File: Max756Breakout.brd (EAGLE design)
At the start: 27 x 27 mm, 8 parts

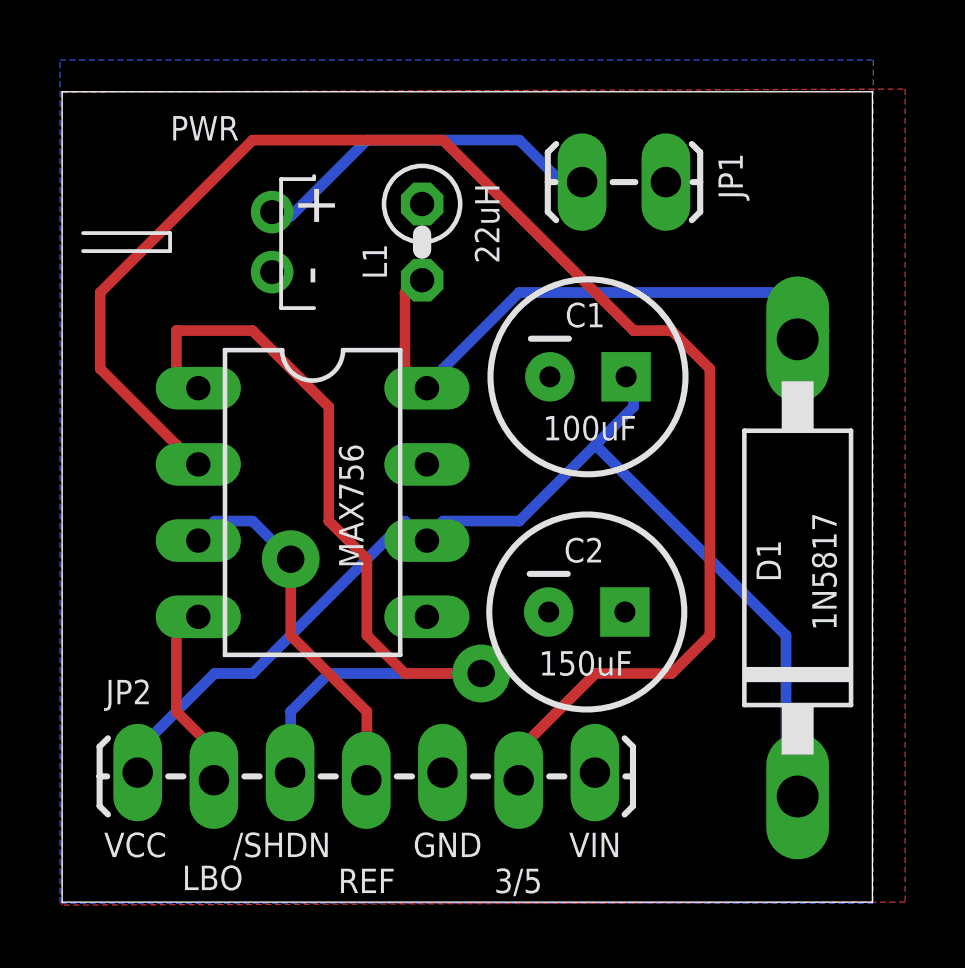
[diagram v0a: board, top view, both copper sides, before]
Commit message: Replaced some parts with better real world representations
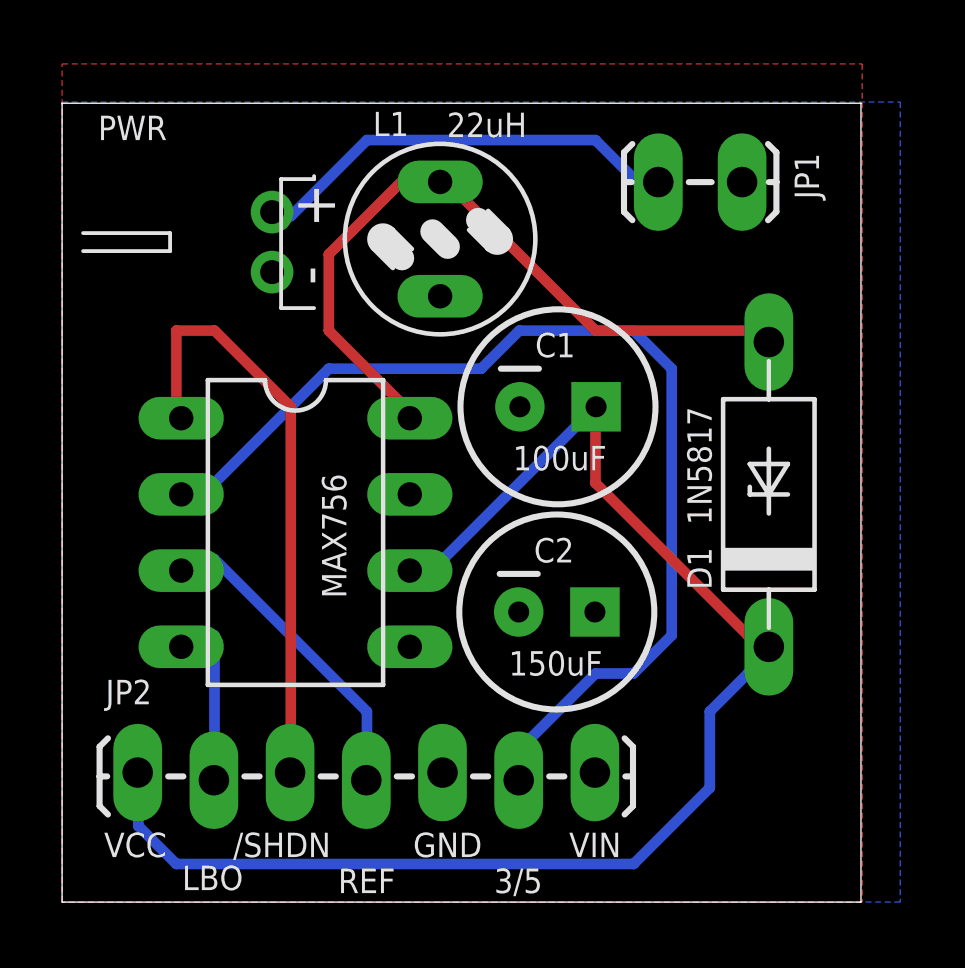
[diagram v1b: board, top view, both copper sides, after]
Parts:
- D1: device adafruit:CB417-15 -> Dek:F126Z12
- L1: device resistor:0207/2V -> Dek:82114R
- moved D1 2.63 mm to (23.6, 13.6)
- moved JP1 2.54 mm to (22.5, 24.0)
- moved C1 1.41 mm to (16.5, 16.5)
- moved MAX756 1.15 mm to (7.78, 12.3)
- moved C2 1.00 mm to (16.5, 9.67)
- moved L1 0.61 mm to (12.6, 22.1), turned to 0 degrees
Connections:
- net L1: now also L1.1; no longer L1.2
- net VIN: now also L1.2; no longer L1.1
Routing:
- net 3/5: track 50.5 -> 35.6 mm
- net /SHDN: track 29.8 -> 20.0 mm, vias 1 -> 0
- net VCC: track 38.7 -> 46.8 mm
- net L1: track 20.3 -> 24.5 mm
- net N$1: track 14.1 -> 16.7 mm
- net REF: track 12.3 -> 10.6 mm, vias 1 -> 0
- added copper zone on layer 16, net GND
- added copper zone on layer 1, net VIN
- removed copper zone on layer 1, net GND
- removed copper zone on layer 16, net VIN
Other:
- board size 27 x 27 mm -> 26.6 x 26.6 mm

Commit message: Changed voltage selector to a jumper
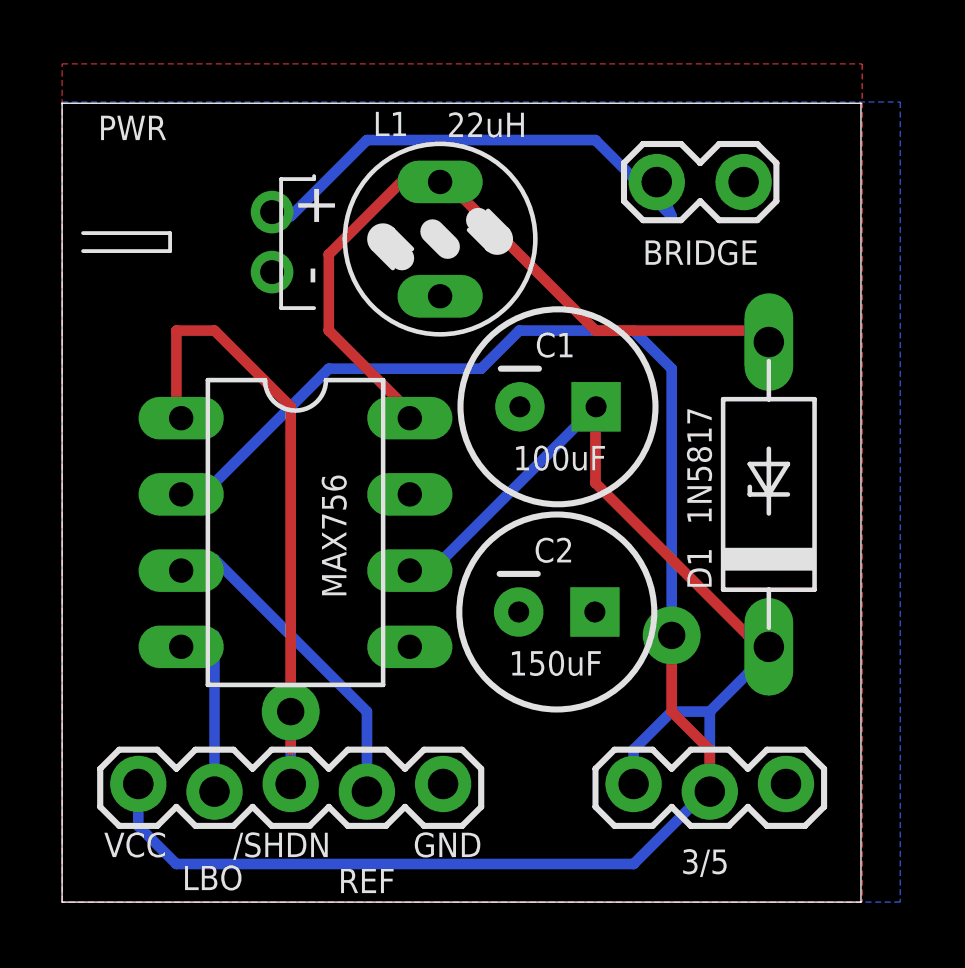
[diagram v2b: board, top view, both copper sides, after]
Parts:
- removed JP1: (no value), SparkFun-Connectors:1X02_LOCK_LONGPADS
- added 3/5: (no value), SparkFun-Connectors:1X03_LOCK
- added BRIDGE: (no value), SparkFun-Connectors:1X02_LOCK
- JP2: device SparkFun-Connectors:1X07_LOCK_LONGPADS -> SparkFun-Connectors:1X05_LOCK
- moved JP2 0.38 mm to (2.54, 3.81)
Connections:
- net 3/5: now also 3/5.2; no longer JP2.6
- net GND: now also 3/5.3
- net N$1: now also BRIDGE.2; no longer JP1.2
- net VCC: now also 3/5.1
- net VIN: now also BRIDGE.1; no longer JP1.1, JP2.7
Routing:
- net VCC: track 46.8 -> 50.7 mm
- net 3/5: track 35.6 -> 33.7 mm, vias 0 -> 1
- net /SHDN: track 20.0 -> 21.8 mm, vias 0 -> 1
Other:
- board text removed: "3/5"
- board text removed: "VIN"

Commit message: Only breakout 2 pins for ease of use
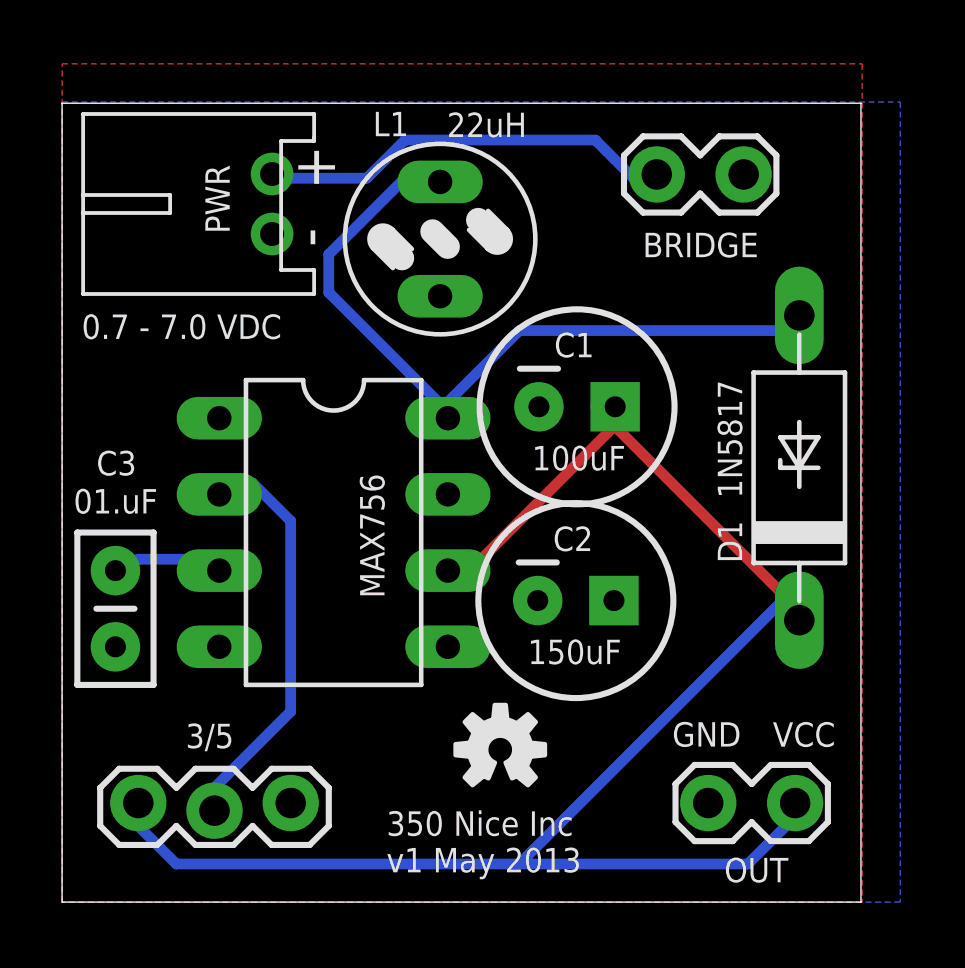
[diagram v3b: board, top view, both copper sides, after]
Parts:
- removed JP2: (no value), SparkFun-Connectors:1X05_LOCK
- added C3: 01.uF, Dek:CAP-PTH-SMALL2
- added OUT: (no value), SparkFun-Connectors:1X02_LOCK
- added U$1: (no value), SparkFun-Aesthetics:OSHW-LOGO-S
- PWR: value PWR -> 0.7 - 7.0VDC; device adafruit:JST-PH-2-THM-RA -> Dek:JST-PH-2-THM-RA
- moved 3/5 16.5 mm to (2.54, 3.17)
- moved D1 1.35 mm to (24.6, 14.5)
- moved MAX756 1.27 mm to (9.05, 12.3)
- moved PWR 1.27 mm to (7.00, 23.3)
- moved C2 0.74 mm to (17.1, 10.1)
- moved C1 0.63 mm to (17.2, 16.5)
- moved BRIDGE 0.25 mm to (22.5, 24.3)
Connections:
- removed net /SHDN: JP2.3, MAX756.1
- net GND: now also C3.2, OUT.2; no longer JP2.5
- net LBO: no longer JP2.2
- net REF: now also C3.1; no longer JP2.4
- net VCC: now also OUT.1; no longer JP2.1
- net VIN: now also MAX756.1
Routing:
- net /SHDN: track 21.8 -> 0.00 mm, vias 1 -> 0
- net 3/5: track 33.7 -> 13.7 mm, vias 1 -> 0
- net REF: track 11.0 -> 3.80 mm
- net VCC: track 50.7 -> 57.2 mm
- net LBO: track 6.38 -> 0.00 mm
- net N$1: track 16.7 -> 13.9 mm
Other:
- board text added: "0.7 - 7.0 VDC"
- board text added: "350 Nice Inc v1 May 2013"
- board text removed: "/SHDN"
- board text removed: "LBO"
- board text removed: "REF"
